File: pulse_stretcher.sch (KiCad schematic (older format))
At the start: 78 parts, among them J1 5VDC, J2 SMA, J3 SMA, U1 MAX1735, U2 MCP1824ST-33, U3 MCP1824ST-25, U4 MC100LVEL31, U5 SY100ELT21L, U6 74LVC1G04, U7 AUC2G04, U8 AUC2G04, U9 AUC2G04

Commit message: Redesigned the PCB
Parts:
- removed C3: 1uC, Capacitor_SMD:C_0603_1608Metric, symbol Device:C
- removed H1, H2, H3, H4: M3, MountingHole:MountingHole_4.3mm_M4, symbol Connector:Screw_Terminal_01x01
- added H1, H2, H3, H4: M4, MountingHole:MountingHole_4.3mm_M4_Pad, symbol Mechanical:MountingHole_Pad
- C12: renamed from C13; symbol pulse_stretcher-rescue:C -> Device:C
- C13: renamed from C14; symbol pulse_stretcher-rescue:C -> pulse_stretcher-rescue:C-pulse_stretcher-rescue
- C15: renamed from C16; symbol pulse_stretcher-rescue:C -> Device:C
- C16: renamed from C17; symbol pulse_stretcher-rescue:C -> pulse_stretcher-rescue:C-pulse_stretcher-rescue
- C19: renamed from C20; symbol pulse_stretcher-rescue:C -> Device:C
- C20: renamed from C21; symbol pulse_stretcher-rescue:C -> pulse_stretcher-rescue:C-pulse_stretcher-rescue
- C21: renamed from C22; symbol pulse_stretcher-rescue:C -> pulse_stretcher-rescue:C-pulse_stretcher-rescue
- C23: renamed from C24; symbol pulse_stretcher-rescue:C -> Device:C
- C24: renamed from C25; symbol pulse_stretcher-rescue:C -> pulse_stretcher-rescue:C-pulse_stretcher-rescue
- C28: renamed from C29; symbol pulse_stretcher-rescue:C -> Device:C
- C31: renamed from C32; symbol pulse_stretcher-rescue:C -> Device:C
- C33: renamed from C34; symbol pulse_stretcher-rescue:C -> pulse_stretcher-rescue:C-pulse_stretcher-rescue
- C34: renamed from C35; symbol pulse_stretcher-rescue:C -> Device:C
- J2, J3: footprint jakub:SMA -> jakub:SMA_5.0mm
- renumbered C11 to C10, C12 to C11, C15 to C14, C18 to C17, C19 to C18, C23 to C22, C26 to C25, C27 to C26, C28 to C27, C30 to C29, C4 to C3, C31 to C30, C33 to C32, C36 to C35, C5 to C4, C6 to C5, C7 to C6, C8 to C7, C9 to C8, C10 to C9
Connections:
- net GND: now also H1.1, H2.1, H3.1, H4.1

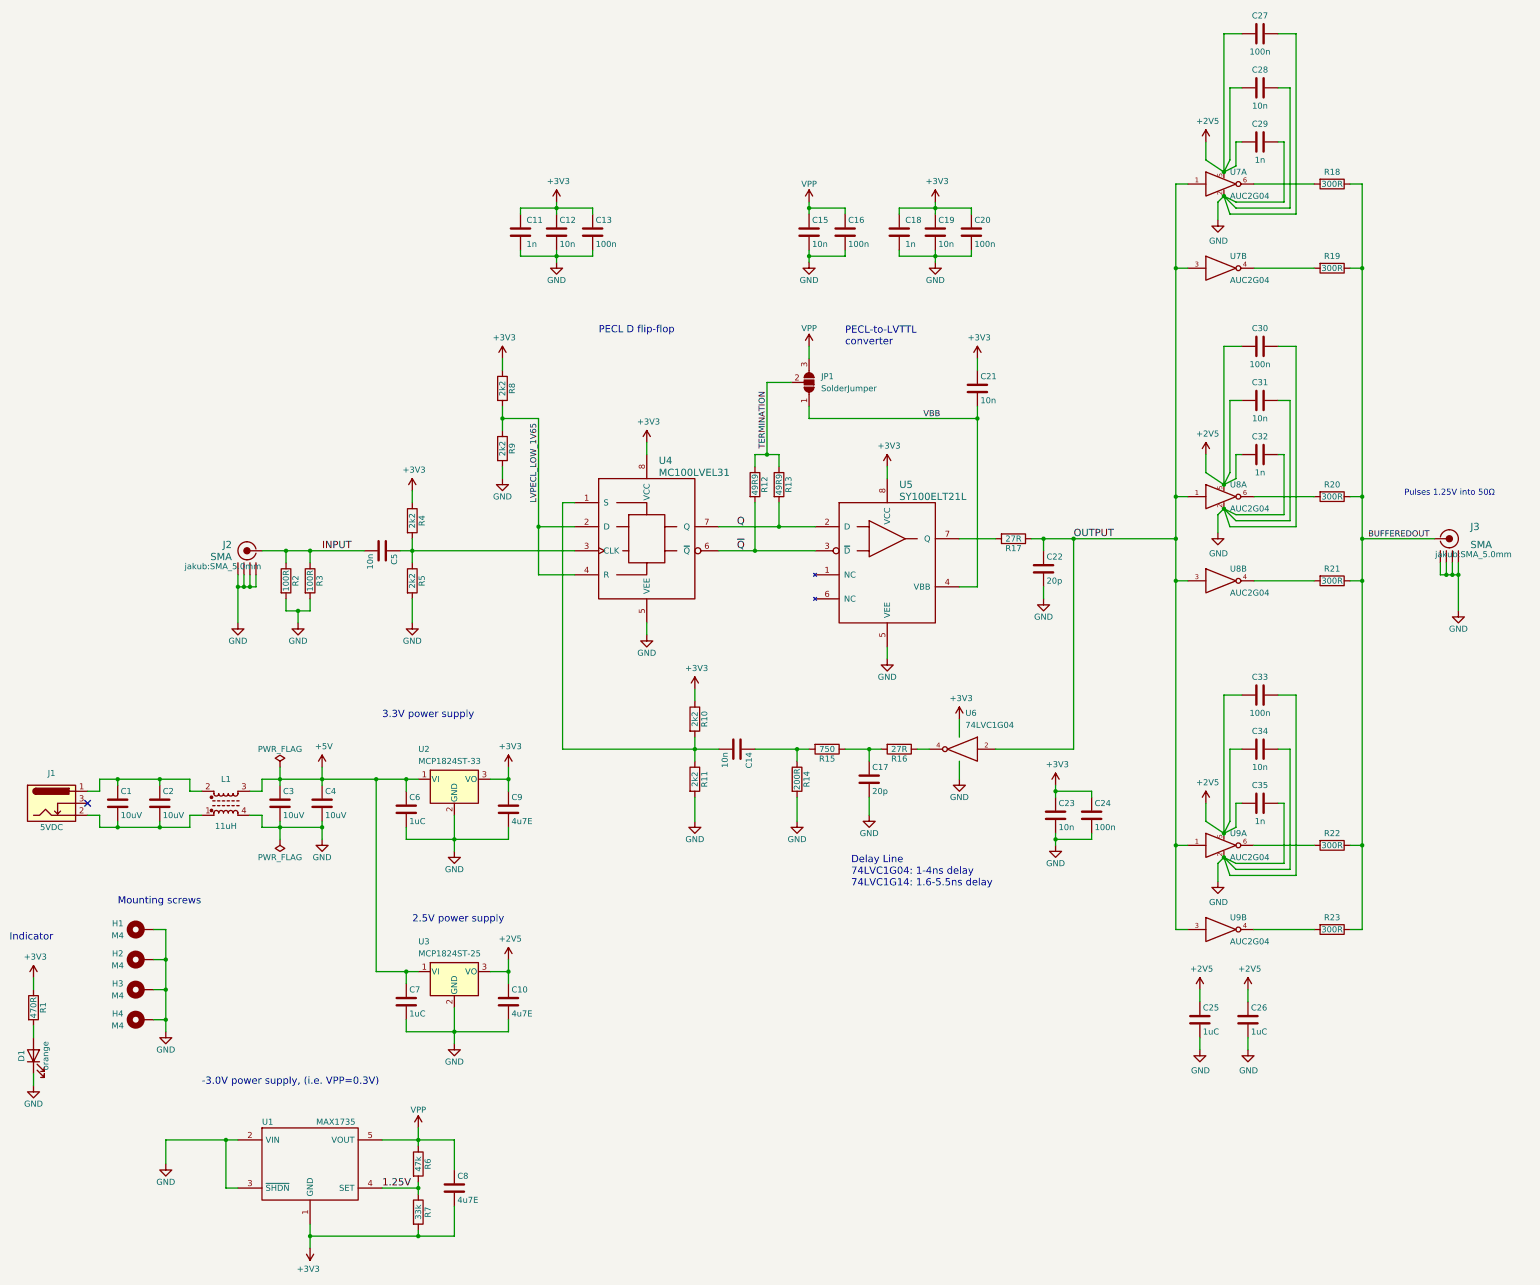
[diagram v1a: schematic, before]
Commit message: Added ~clock_enable
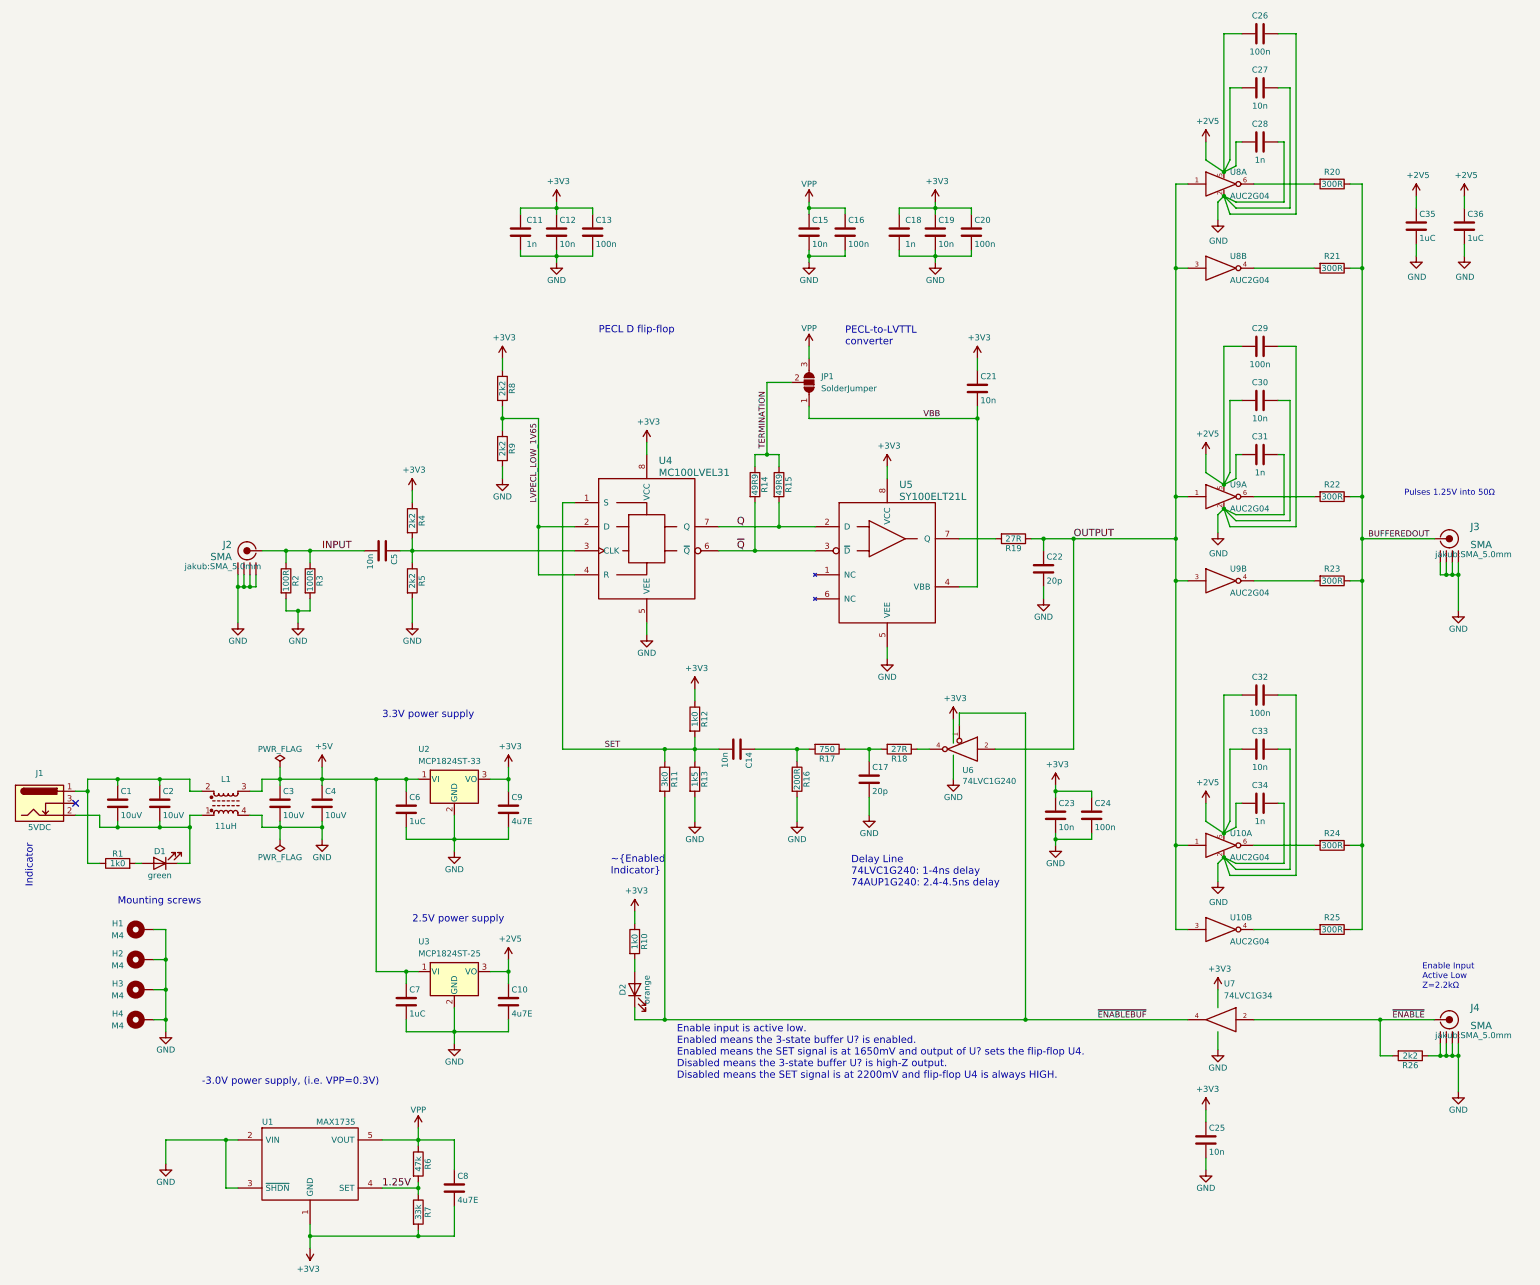
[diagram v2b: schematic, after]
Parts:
- removed U6: 74LVC1G04, Package_TO_SOT_SMD:SOT-23-5_HandSoldering, symbol 74xGxx:74LVC1G04
- added C25: 10n, Capacitor_SMD:C_0402_1005Metric, symbol Device:C
- added D2: orange, LED_THT:LED_D3.0mm, symbol Device:LED
- added J4: SMA, jakub:SMA_5.0mm, symbol jakub:SMA
- added R10: 1k0, Resistor_SMD:R_0603_1608Metric, symbol Device:R
- added R11: 3k0, Resistor_SMD:R_0603_1608Metric, symbol Device:R
- added R26: 2k2, Resistor_SMD:R_0603_1608Metric, symbol Device:R
- added U6: 74LVC1G240, Package_TO_SOT_SMD:SOT-23-5, symbol 74xGxx:74LVC1G240
- added U7: 74LVC1G34, Package_TO_SOT_SMD:SOT-23-5, symbol 74xGxx:74LVC1G34
- D1: value orange -> green
- R1: value 470R -> 1k0; Note 470Ω/1% 0603 resistor -> 1.0kΩ/1% 0603 resistor; Order Code 2447374 -> 9238484; Part Number MCWR06X4700FTL -> RC0603FR-071KL
- R12: renamed from R10; value 2k2 -> 1k0; Note 2.2kΩ/1% 0603 resistor -> 1.0kΩ/1% 0603 resistor; Order Code 9238522 -> 9238484; Part Number RC0603FR-072K2L -> RC0603FR-071KL
- R13: renamed from R11; value 2k2 -> 1k5; Note 2.2kΩ/1% 0603 resistor -> 1.5kΩ/1% 0603 resistor; Order Code 9238522 -> 9238506; Part Number RC0603FR-072K2L -> RC0603FR-071K5L
- renumbered C27 to C26, C28 to C27, C29 to C28, C30 to C29, C31 to C30, C32 to C31, C33 to C32, C34 to C33, C35 to C34, C25 to C35, C26 to C36, R12 to R14, R13 to R15, R14 to R16, R15 to R17, R16 to R18, R17 to R19, R18 to R20, R19 to R21, R20 to R22, R21 to R23, R22 to R24, R23 to R25, U9 to U10, U7 to U8, U8 to U9
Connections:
- net +3V3: now also C25.1, R10.1, U6.5 (VCC), U7.5 (VCC); no longer R1.1
- net GND: now also C25.2, J4.2 (GND1), J4.3 (GND2), J4.4 (GND3), J4.5 (GND4), R26.1, U6.3 (GND), U7.3 (GND); no longer D1.1 (K)
- net OUTPUT: now also U6.2
- net SET: now reaches C14.2, R12.2, R13.1, U4.1 (S)
- net SET: now also R11.1
- net at C1.1, C2.1, J1.1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: now also R1.1
- net at C1.2, C2.2, J1.2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: now also D1.1 (K)
- net at R18.1: now also U6.4
- new net: D2.2 (A), R10.2
- new net ~ENABLE: J4.1 (RF), R26.2, U7.2
- new net ~ENABLEBUF: D2.1 (K), R11.2, U6.1, U7.4
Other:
- note added: "Delay Line\n74LVC1G240: 1-4ns delay\n74AUP1G240: 2.4-4.5ns delay"
- note added: "Enable Input\nActive Low\nZ=2.2kΩ"
- note added: "Enable input is active low.\nEnabled means the 3-state buffer U? is enabled.\nEnabled means the SET signal is at 1650mV and output of U? sets the flip-flop U4.\nDisabled means the 3-state buffer U? is high-Z output.\nDisabled means the SET signal is at 2200mV and flip-flop U4 is always HIGH.\n"
- note added: "~Enabled\nIndicator"
- note removed: "Delay Line\n74LVC1G04: 1-4ns delay\n74LVC1G14: 1.6-5.5ns delay"
- moved on the sheet: C35, C36, D1, J1, R1

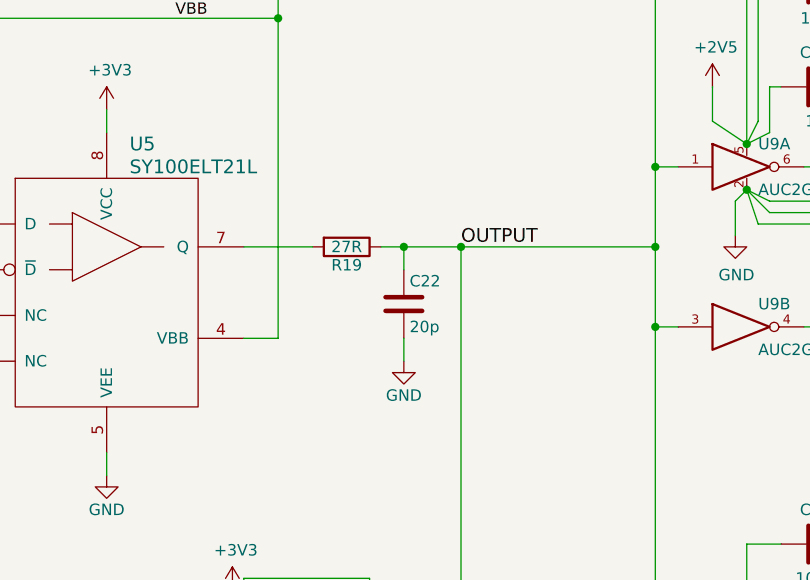
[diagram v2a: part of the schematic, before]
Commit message: Added comment about RC filter being optional
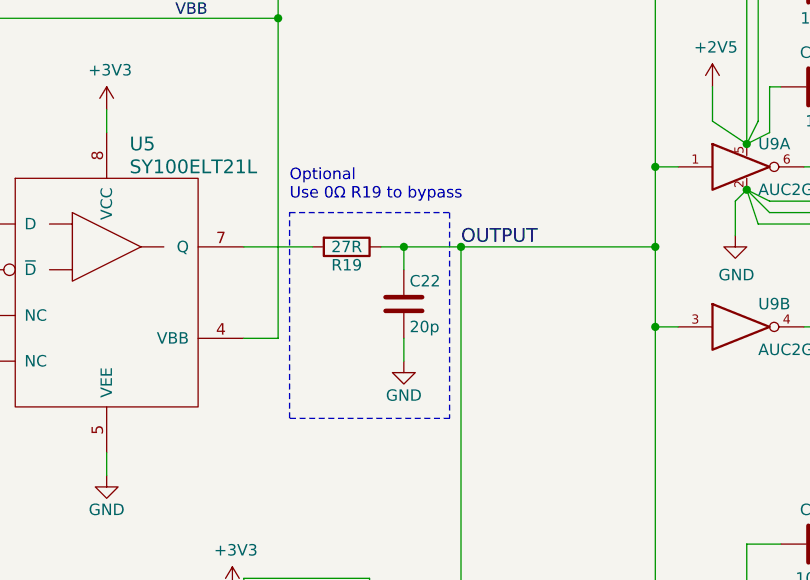
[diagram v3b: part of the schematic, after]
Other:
- note added: "Optional\nUse 0Ω R19 to bypass"
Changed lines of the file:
@@
 Wire Wire Line
 	1450 7000 1700 7000
+Wire Notes Line
+	8900 4850 9600 4850
+Wire Notes Line
+	9600 4850 9600 5750
+Wire Notes Line
+	9600 5750 8900 5750
+Wire Notes Line
+	8900 5750 8900 4850
+Text Notes 8900 4800 0    50   ~ 0
+Optional\nUse 0Ω R19 to bypass
 $EndSCHEMATC

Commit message: Production run
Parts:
- C17, C22: footprint Capacitor_SMD:C_0402_1005Metric -> Capacitor_SMD:C_0603_1608Metric; Note 20pF/50V C0G 0402 ceramic capacitor -> 20pF/50V C0G 0603 ceramic capacitor; Order Code 1758948 -> 2627461; Package 0402 -> 0603; Part Number MC0402N200J500CT -> MC0603N200J500CT
- C26, C29: Manufacturer Multicomp -> TDK; Order Code 1759122 -> 2522004; Part Number MC0603B104K500 -> C1608X7R1H104M080AA
- R17: value 750 -> 750R
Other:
- note added: "Enable Input\nActive Low\nZ=2.2kΩ\nHigh 2V-5V"
- note added: "Enable input is active low.\nEnabled means the 3-state buffer U6 is enabled.\nEnabled means the SET signal is at 1650mV and output of U6 sets the flip-flop U4.\nDisabled means the 3-state buffer U6 is high-Z output.\nDisabled means the SET signal is at 2200mV and flip-flop U4 is always HIGH.\n"
- note removed: "Enable Input\nActive Low\nZ=2.2kΩ"
- note removed: "Enable input is active low.\nEnabled means the 3-state buffer U? is enabled.\nEnabled means the SET signal is at 1650mV and output of U? sets the flip-flop U4.\nDisabled means the 3-state buffer U? is high-Z output.\nDisabled means the SET signal is at 2200mV and flip-flop U4 is always HIGH.\n"
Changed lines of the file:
@@
 F 2 "Capacitor_SMD:C_0603_1608Metric" H 11238 650 50  0001 C CNN
 F 3 "~" H 11200 800 50  0001 C CNN
-F 4 "MC0603B104K500" H 11200 800 50  0001 C CNN "Part Number"
-F 5 "Multicomp" H 11200 800 50  0001 C CNN "Manufacturer"
+F 4 "C1608X7R1H104M080AA" H 11200 800 50  0001 C CNN "Part Number"
+F 5 "TDK" H 11200 800 50  0001 C CNN "Manufacturer"
 F 6 "0603" H 11200 800 50  0001 C CNN "Package"
 F 7 "Farnell" H 11200 800 50  0001 C CNN "Supplier"
-F 8 "1759122" H 11200 800 50  0001 C CNN "Order Code"
+F 8 "2522004" H 11200 800 50  0001 C CNN "Order Code"
 F 9 "100nF/50V X7R 0603 ceramic capacitor" H 11200 800 50  0001 C CNN "Note"
 F 10 "Seeed OPL" H 11200 800 50  0001 C CNN "Alt. Supplier"
@@
 F 0 "C17" H 7975 7100 50  0000 L CNN
 F 1 "20p" H 7975 6900 50  0000 L CNN
-F 2 "Capacitor_SMD:C_0402_1005Metric" H 7988 6850 50  0001 C CNN
+F 2 "Capacitor_SMD:C_0603_1608Metric" H 7988 6850 50  0001 C CNN
 F 3 "" H 7950 7000 50  0000 C CNN
-F 4 "MC0402N200J500CT" H 7950 7000 60  0001 C CNN "Part Number"
+F 4 "MC0603N200J500CT" H 7950 7000 60  0001 C CNN "Part Number"
 F 5 "Multicomp" H 7950 7000 60  0001 C CNN "Manufacturer"
-F 6 "0402" H 7950 7000 60  0001 C CNN "Package"
+F 6 "0603" H 7950 7000 60  0001 C CNN "Package"
 F 7 "Farnell" H 7950 7000 60  0001 C CNN "Supplier"
-F 8 "1758948" H 7950 7000 60  0001 C CNN "Order Code"
-F 9 "20pF/50V C0G 0402 ceramic capacitor" H 7950 7000 60  0001 C CNN "Note"
+F 8 "2627461" H 7950 7000 60  0001 C CNN "Order Code"
+F 9 "20pF/50V C0G 0603 ceramic capacitor" H 7950 7000 60  0001 C CNN "Note"
 	1    7950 7000
 	1    0    0    -1
@@
 F 0 "C22" H 9425 5350 50  0000 L CNN
 F 1 "20p" H 9425 5150 50  0000 L CNN
-F 2 "Capacitor_SMD:C_0402_1005Metric" H 9438 5100 50  0001 C CNN
+F 2 "Capacitor_SMD:C_0603_1608Metric" H 9438 5100 50  0001 C CNN
 F 3 "" H 9400 5250 50  0000 C CNN
-F 4 "MC0402N200J500CT" H 9400 5250 60  0001 C CNN "Part Number"
+F 4 "MC0603N200J500CT" H 9400 5250 60  0001 C CNN "Part Number"
 F 5 "Multicomp" H 9400 5250 60  0001 C CNN "Manufacturer"
-F 6 "0402" H 9400 5250 60  0001 C CNN "Package"
+F 6 "0603" H 9400 5250 60  0001 C CNN "Package"
 F 7 "Farnell" H 9400 5250 60  0001 C CNN "Supplier"
-F 8 "1758948" H 9400 5250 60  0001 C CNN "Order Code"
-F 9 "20pF/50V C0G 0402 ceramic capacitor" H 9400 5250 60  0001 C CNN "Note"
+F 8 "2627461" H 9400 5250 60  0001 C CNN "Order Code"
+F 9 "20pF/50V C0G 0603 ceramic capacitor" H 9400 5250 60  0001 C CNN "Note"
 	1    9400 5250
 	1    0    0    -1
@@
 F 2 "Capacitor_SMD:C_0603_1608Metric" H 11238 3250 50  0001 C CNN
 F 3 "~" H 11200 3400 50  0001 C CNN
-F 4 "MC0603B104K500" H 11200 3400 50  0001 C CNN "Part Number"
-F 5 "Multicomp" H 11200 3400 50  0001 C CNN "Manufacturer"
+F 4 "C1608X7R1H104M080AA" H 11200 3400 50  0001 C CNN "Part Number"
+F 5 "TDK" H 11200 3400 50  0001 C CNN "Manufacturer"
 F 6 "0603" H 11200 3400 50  0001 C CNN "Package"
 F 7 "Farnell" H 11200 3400 50  0001 C CNN "Supplier"
-F 8 "1759122" H 11200 3400 50  0001 C CNN "Order Code"
+F 8 "2522004" H 11200 3400 50  0001 C CNN "Order Code"
 F 9 "100nF/50V X7R 0603 ceramic capacitor" H 11200 3400 50  0001 C CNN "Note"
 F 10 "Seeed OPL" H 11200 3400 50  0001 C CNN "Alt. Supplier"
@@
 P 7600 6750
 F 0 "R17" V 7680 6750 50  0000 C CNN
-F 1 "750" V 7600 6750 50  0000 C CNN
+F 1 "750R" V 7600 6750 50  0000 C CNN
 F 2 "Resistor_SMD:R_0603_1608Metric" V 7530 6750 50  0001 C CNN
 F 3 "" H 7600 6750 50  0000 C CNN
@@
 ~ENABLEBUF
 Text Notes 6350 9500 0    60   ~ 0
-Enable input is active low.\nEnabled means the 3-state buffer U? is enabled.\nEnabled means the SET signal is at 1650mV and output of U? sets the flip-flop U4.\nDisabled means the 3-state buffer U? is high-Z output.\nDisabled means the SET signal is at 2200mV and flip-flop U4 is always HIGH.\n
+Enable input is active low.\nEnabled means the 3-state buffer U6 is enabled.\nEnabled means the SET signal is at 1650mV and output of U6 sets the flip-flop U4.\nDisabled means the 3-state buffer U6 is high-Z output.\nDisabled means the SET signal is at 2200mV and flip-flop U4 is always HIGH.\n
 $Comp
 L pulse_stretcher-rescue:GND-pulse_stretcher-rescue #PWR045
@@
 $EndComp
 Text Notes 12550 8750 0    50   ~ 0
-Enable Input\nActive Low\nZ=2.2kΩ
+Enable Input\nActive Low\nZ=2.2kΩ\nHigh 2V-5V
 Text Label 5750 6750 0    50   ~ 0
 SET
